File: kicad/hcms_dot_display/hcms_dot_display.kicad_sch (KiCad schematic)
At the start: 40 parts, among them J1 Conn_01x11, J2 USB_C_Receptacle_USB2.0, J3 Conn_01x11, J4 Conn_01x10_Female, J5 Conn_01x10_Male, Q1 Q_PMOS_DSG, Q2 Q_PMOS_DSG, Q3 Q_PMOS_DSG, Q4 Q_PMOS_DSG, Q5 Q_PMOS_DSG, SW2 SW_SPST, U1 ATtiny824-SSF, U2 FT231XS

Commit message: progress from 0406
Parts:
- added J?: Conn_01x10_Female, Connector_PinHeader_2.54mm:PinHeader_1x10_P2.54mm_Vertical, symbol Connector:Conn_01x10_Female
- added J?: Conn_01x10_Male, Connector_PinHeader_2.54mm:PinHeader_1x10_P2.54mm_Vertical, symbol Connector:Conn_01x10_Male
- added Q?: (no value), symbol Device:Q_NMOS_GSD
- added U?: (no value), symbol hcms_dot_display:MIC5018
- SW2: value SW_SPST -> (none)
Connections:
- net +5V: now also J?.1 (Pin_1), J?.1 (Pin_1)
- net CLK: now also J?.8 (Pin_8), J?.8 (Pin_8)
- net GND: now also J?.10 (Pin_10), J?.10 (Pin_10)
- net MCU_COL_1: now also J?.2 (Pin_2), J?.2 (Pin_2)
- net MCU_COL_2: now also J?.3 (Pin_3), J?.3 (Pin_3)
- net MCU_COL_3: now also J?.4 (Pin_4), J?.4 (Pin_4)
- net MCU_COL_4: now also J?.5 (Pin_5), J?.5 (Pin_5)
- net MCU_COL_5: now also J?.6 (Pin_6), J?.6 (Pin_6)
- net MCU_DATA: now also J?.9 (Pin_9), J?.9 (Pin_9)
- net nBLNK: now also U1.3 (XTAL2/PB1), J?.7 (Pin_7), J?.7 (Pin_7); no longer U1.4 (~{RESET}/PB3)
- new net COL_PWM: U1.4 (~{RESET}/PB3), U?.4 (CTRL)
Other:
- note added: "DMN2046U"
- note added: "MIC5018YM4-TR"
- moved on the sheet: C1, C10, C11, C2, C3, D1A, D1B, J3, J4, J5, Q1, Q2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

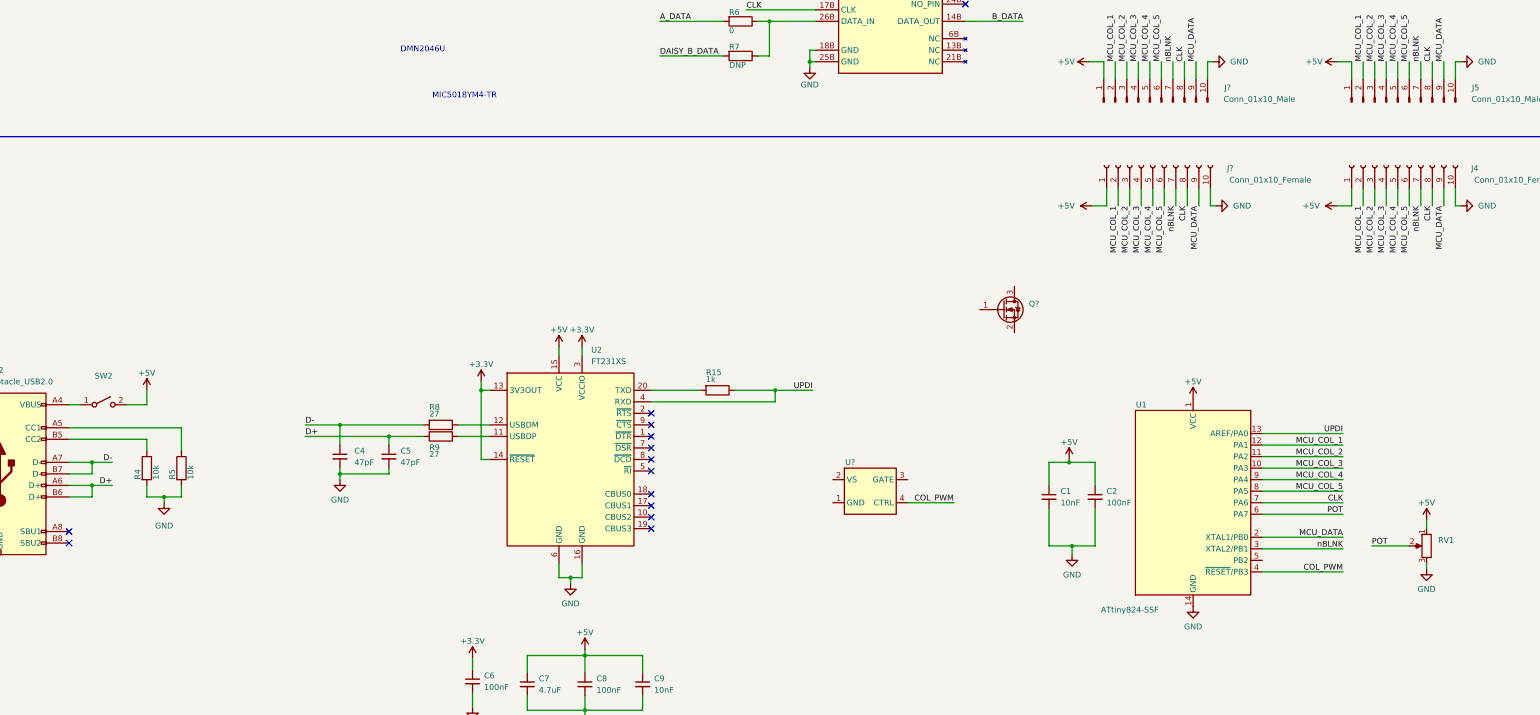
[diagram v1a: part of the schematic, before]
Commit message: updated micro to have more i/o
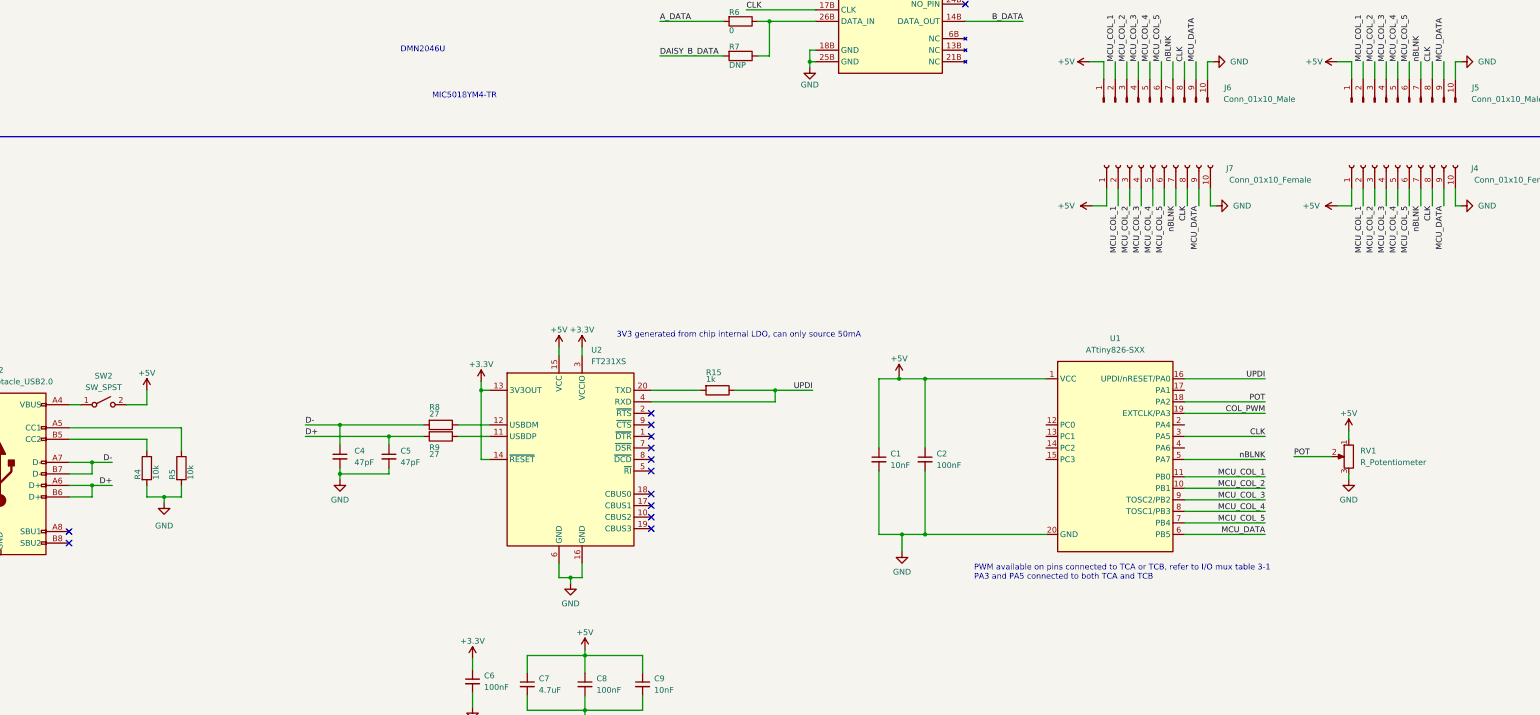
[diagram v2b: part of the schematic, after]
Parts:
- removed Q?: (no value), symbol Device:Q_NMOS_GSD
- removed U1: ATtiny824-SSF, Package_SO:SOIC-14_3.9x8.7mm_P1.27mm, symbol MCU_Microchip_ATtiny:ATtiny84-20SS
- removed U?: (no value), symbol hcms_dot_display:MIC5018
- added U1: ATtiny826-SXX, Package_SO:SOIC-14_3.9x8.7mm_P1.27mm, symbol hcms_dot_display:ATtiny826-SXX
- RV1: value (none) -> R_Potentiometer; footprint (none) -> hcms:TRIM_3352T-1-201LF
- SW2: value (none) -> SW_SPST; footprint (none) -> Button_Switch_SMD:SW_DIP_SPSTx03_Slide_KingTek_DSHP03TS_W7.62mm_P1.27mm
- gave numbers to parts that had none: 2
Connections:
- net +5V: now also U1.1 (VCC)
- net CLK: now also U1.3 (PA5)
- net COL_PWM: now also U1.19 (EXTCLK/PA3)
- net GND: now also U1.20 (GND)
- net MCU_COL_1: now also U1.11 (PB0)
- net MCU_COL_2: now also U1.10 (PB1)
- net MCU_COL_3: now also U1.9 (TOSC2/PB2)
- net MCU_COL_4: now also U1.8 (TOSC1/PB3)
- net MCU_COL_5: now also U1.7 (PB4)
- net MCU_DATA: now also U1.6 (PB5)
- net POT: now also U1.18 (PA2)
- net UPDI: now also U1.16 (UPDI/nRESET/PA0)
- net nBLNK: now also U1.5 (PA7)
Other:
- note added: "3V3 generated from chip internal LDO, can only source 50mA"
- note added: "PWM available on pins connected to TCA or TCB, refer to I/O mux table 3-1 PA3 and PA5 connected to both TCA and TCB"
- moved on the sheet: C1, C2, RV1
